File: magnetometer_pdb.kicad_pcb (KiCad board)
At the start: 2 copper layers, 98 x 87.5 mm, 80 parts, among them J1 Screw_Terminal_01x02, J10 Screw_Terminal_01x02, J11 Screw_Terminal_01x02, J12 Screw_Terminal_01x02, J13 Screw_Terminal_01x02, J14 Screw_Terminal_01x02, J15 Conn_01x02_Pin, J2 Screw_Terminal_01x02, J3 Screw_Terminal_01x02, J4 Screw_Terminal_01x02, J5 Screw_Terminal_01x02, J6 Conn_01x02_Pin, J7 Conn_01x02_Pin, J8 Conn_01x02_Pin, J9 Screw_Terminal_01x02, U1 TPS56528DDA, U2 L78L09_SO8

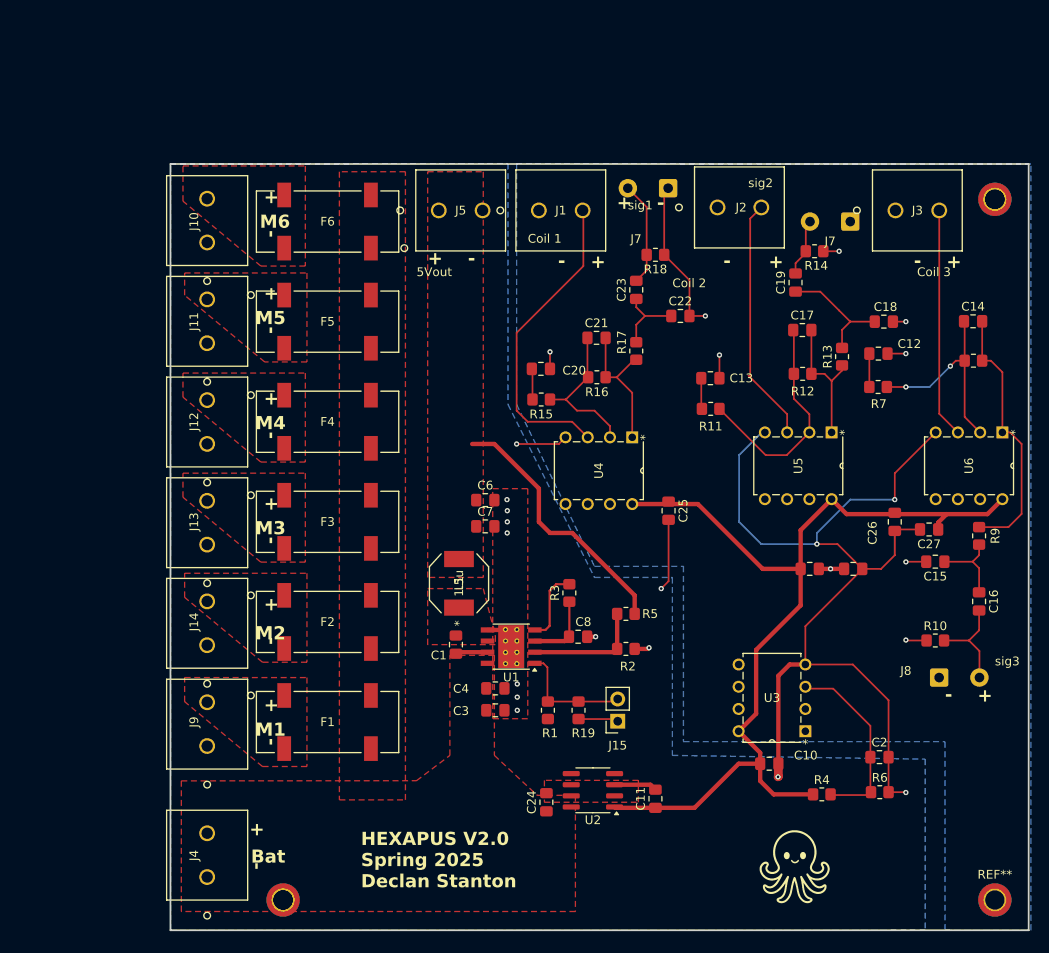
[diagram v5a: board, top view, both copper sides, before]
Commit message: Simplified Schematic and finished PCB
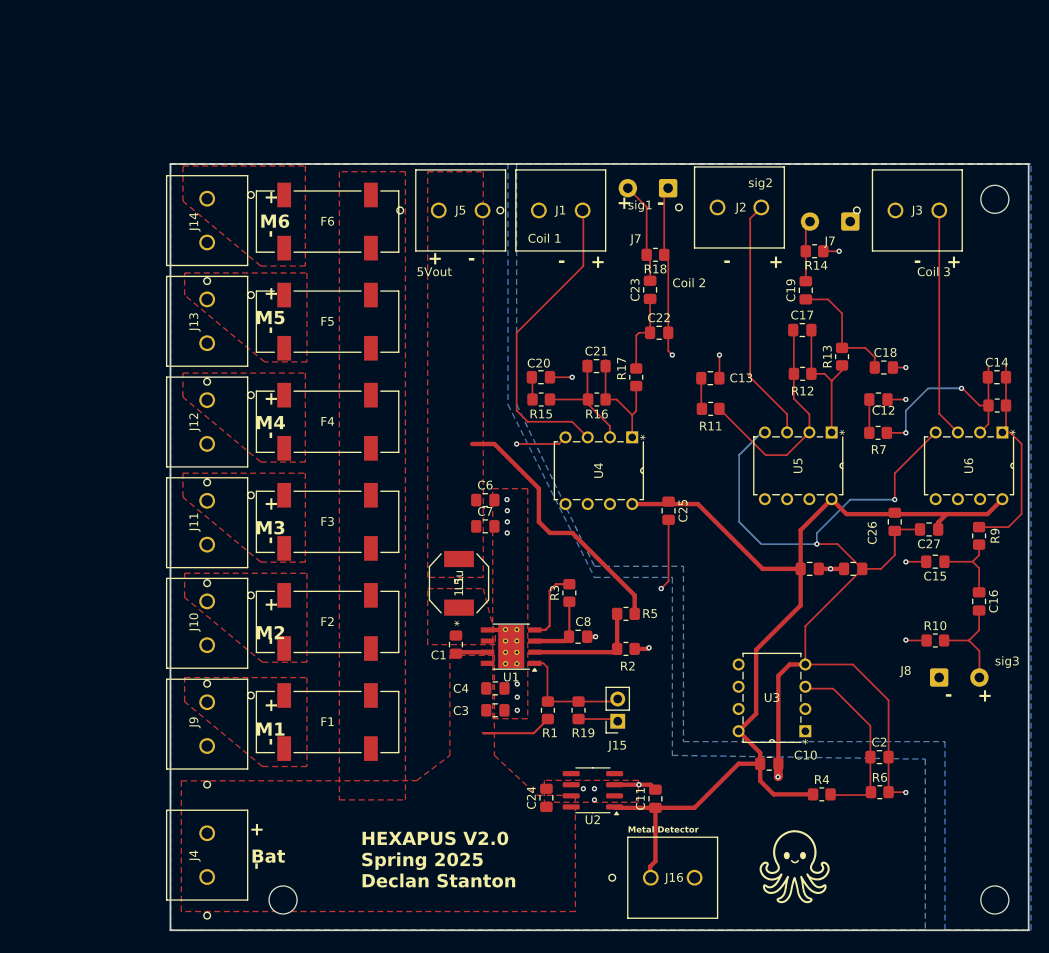
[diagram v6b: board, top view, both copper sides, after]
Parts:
- removed ? (x2): , 
- removed the REF** at (111.8, 19.1)
- removed the REF** at (30.5, 99.1)
- removed the REF** at (111.8, 99.1)
- added J16: Screw_Terminal_01x02, Connector_PinHeader_2.00mm:2_Pin_Screw_Term, F.Cu at (72.5, 96.5)
- added REF**: MountingHole_3.2mm_M3, MountingHole:MountingHole_3.2mm_M3, F.Cu at (111.8, 99.1)
- added REF**: MountingHole_3.2mm_M3, MountingHole:MountingHole_3.2mm_M3, F.Cu at (30.5, 99.1)
- added REF**: MountingHole_3.2mm_M3, MountingHole:MountingHole_3.2mm_M3, F.Cu at (111.8, 19.1)
- moved C14 6.94 mm to (112.0, 39.4)
- moved R8 5.80 mm to (112.0, 42.6)
- moved C18 5.24 mm to (99.1, 38.3)
- moved R7 5.24 mm to (98.4, 45.7)
- moved C12 5.24 mm to (98.5, 41.9)
- moved C21 3.23 mm to (66.3, 38.1)
- moved C22 3.09 mm to (73.4, 34.3)
- moved R17 3.00 mm to (70.8, 39.4)
- moved R16 2.54 mm to (66.3, 41.9)
- moved C23 1.58 mm to (72.4, 29.4)
- moved C19 1.47 mm to (90.2, 29.4)
- moved C20 0.96 mm to (59.9, 39.4)
- moved C24 0.50 mm to (60.5, 87.4)
- turned F6 to 0 degrees
- renumbered J14 to J10, J13 to J11, J11 to J13, J10 to J14
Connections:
- net 5V_out renamed 5V_OUT
- net 9V_out renamed /12_9_Linear_Reg/9V_OUT
- net Coil_1_sig_out renamed /C1_OUT
- net Coil_2_sig_out renamed /C2_OUT
- net Coil_3_sig_out renamed /C3_OUT
- net GND renamed /12_9_Linear_Reg/V_GND
- net Net-(J1-Pin_2) renamed /3_AX_Magnetometer/C1_IN
- net Net-(J2-Pin_2) renamed /3_AX_Magnetometer/C2_IN
- net Net-(J3-Pin_2) renamed /3_AX_Magnetometer/C3_IN
- net Vin renamed +BATT
- F1 pad 1: /M1_out -> /M1_OUT
- J10 pad 2: unconnected-(J14-Pin_2-Pad2) -> /M2_OUT
- J11 pad 2: unconnected-(J13-Pin_2-Pad2) -> /M3_OUT
- J12 pad 2: unconnected-(J12-Pin_2-Pad2) -> /M4_OUT
- J13 pad 2: unconnected-(J11-Pin_2-Pad2) -> /M5_OUT
- J14 pad 2: unconnected-(J10-Pin_2-Pad2) -> /M6_OUT
- J9 pad 2: unconnected-(J9-Pin_2-Pad2) -> /M1_OUT
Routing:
- net +BATT: track 0.00 -> 9.32 mm
- net /12_9_Linear_Reg/9V_OUT: track 108.5 -> 116.7 mm
- net Net-(C14-Pad2): track 30.4 -> 23.9 mm
- net Net-(U4--): track 17.4 -> 14.1 mm
- net (no net): track 0.00 -> 2.54 mm
- net Net-(C21-Pad2): track 16.4 -> 14.3 mm
- net Net-(U6--): track 23.2 -> 24.1 mm
- net Net-(C20-Pad2): track 3.42 -> 2.57 mm
- net Net-(C22-Pad1): track 8.77 -> 9.34 mm
- net Bat_GND: vias 15 -> 19
- added copper zone on F.Cu, net /M1_OUT
- removed copper zone on F.Cu, net /M1_out
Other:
- board text added: "Metal Detector"

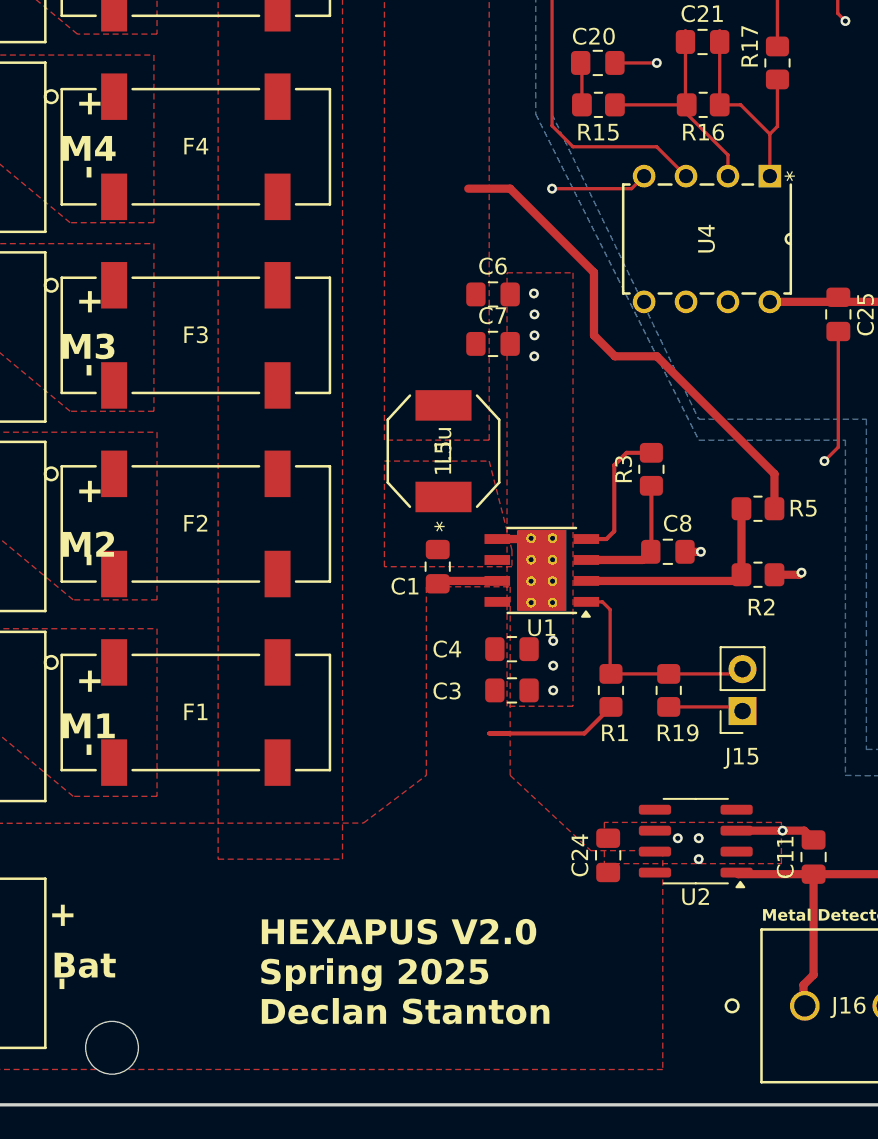
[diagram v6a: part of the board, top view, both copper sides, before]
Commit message: Added bypass caps for 5V output and battery to protect from in rush and back emf
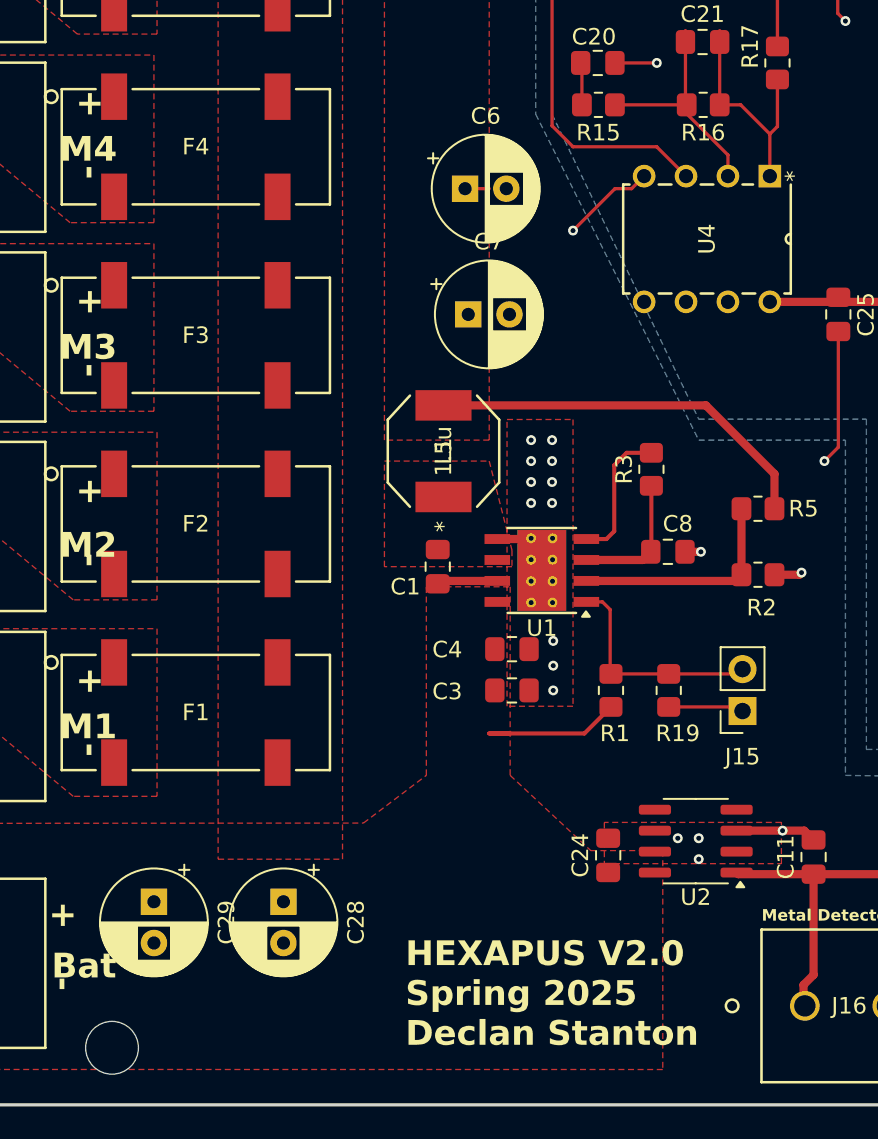
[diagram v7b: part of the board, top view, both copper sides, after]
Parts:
- added C28: 100u, Capacitor_THT:CP_Radial_D6.3mm_P2.50mm, F.Cu at (40.9, 90.2)
- added C29: C_Polarized_US, Capacitor_THT:CP_Radial_D6.3mm_P2.50mm, F.Cu at (33.0, 90.2)
- C6, C7: footprint Capacitor_SMD:C_0805_2012Metric_Pad1.18x1.45mm_HandSolder -> Capacitor_THT:CP_Radial_D6.3mm_P2.50mm
- moved C6 6.63 mm to (51.9, 47.0)
- moved C7 2.34 mm to (52.1, 54.6)
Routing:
- net 5V_OUT: track 31.3 -> 25.2 mm
- net Bat_GND: track 141.8 -> 141.6 mm, vias 19 -> 23
